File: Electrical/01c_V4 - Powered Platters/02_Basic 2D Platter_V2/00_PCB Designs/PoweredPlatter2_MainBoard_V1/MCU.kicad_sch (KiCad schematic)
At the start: 11 parts, among them J3 M20-7920242R, U1 STM32C071KBTx, Y1 16Mhz, 3.2 x 2.5

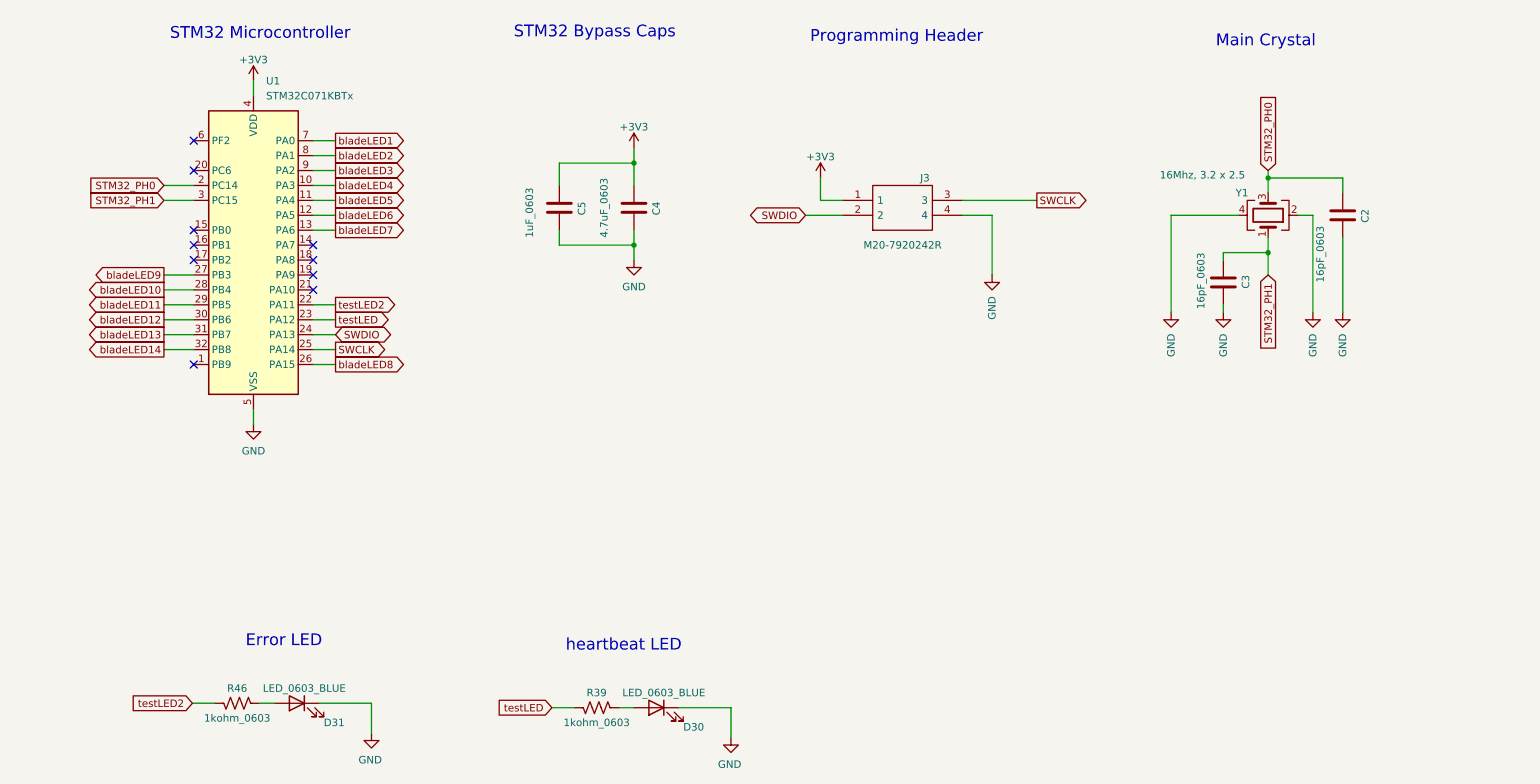
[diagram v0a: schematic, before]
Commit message: second powered platter main PCB designed and ready for CNC milling
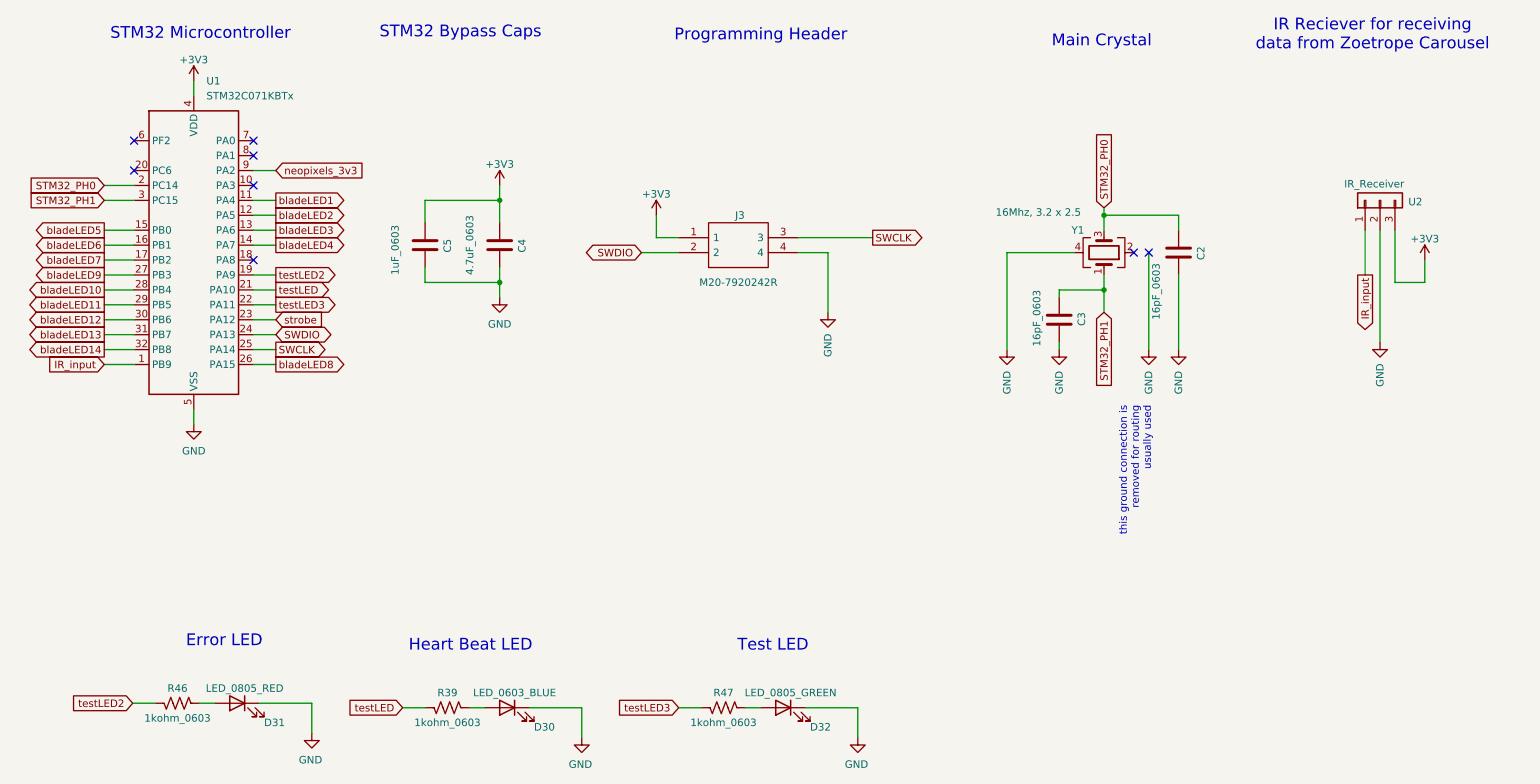
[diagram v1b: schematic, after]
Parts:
- added D32: LED_0805_GREEN, LED_SMD:LED_0805_2012Metric, symbol Device:LED
- added R47: 1kohm_0603, Resistor_SMD:R_0603_1608Metric, symbol Device:R_US
- added U2: IR_Receiver, Connector_PinHeader_2.54mm:PinHeader_1x03_P2.54mm_Vertical, symbol Connector_Generic:Conn_01x03
- D31: value LED_0603_BLUE -> LED_0805_RED; footprint LED_SMD:LED_0603_1608Metric -> LED_SMD:LED_0805_2012Metric
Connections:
- net +3V3: now also U2.3 (Pin_3)
- net GND: now also D32.1 (K), U2.2 (Pin_2); no longer Y1.2
- net bladeLED1: now also U1.11 (PA4); no longer U1.7 (PA0)
- net bladeLED2: now also U1.12 (PA5); no longer U1.8 (PA1)
- net bladeLED3: now also U1.13 (PA6); no longer U1.9 (PA2)
- net bladeLED4: now also U1.14 (PA7); no longer U1.10 (PA3)
- net bladeLED5: now also U1.15 (PB0); no longer U1.11 (PA4)
- net bladeLED6: now also U1.16 (PB1); no longer U1.12 (PA5)
- net bladeLED7: now also U1.17 (PB2); no longer U1.13 (PA6)
- net testLED: now also U1.21 (PA10); no longer U1.23 (PA12)
- net testLED2: now also U1.19 (PA9); no longer U1.22 (PA11)
- net IR_input: now reaches U1.1 (PB9)
- net IR_input: now also U2.1 (Pin_1)
- new net: D32.2 (A), R47.1
- new net neopixels_3v3: U1.9 (PA2)
- new net strobe: U1.23 (PA12)
- new net testLED3: R47.2, U1.22 (PA11)
- no-connect marks 10 -> 8
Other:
- note added: "Heart Beat LED"
- note added: "IR Reciever for receiving data from Zoetrope Carousel"
- note added: "Test LED"
- note added: "this ground connection is removed for routing usually used"
- note removed: "heartbeat LED"
- moved on the sheet: C2, C3, C4, C5, D30, D31, J3, R39, R46, Y1

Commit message: small updates - pushing to move to other computer
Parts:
- C2, C3, Y1: now not fitted
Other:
- note added: "DNP - Traces broke during CNC milling Use internal oscilator to save the headache"
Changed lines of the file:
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@@
 		)
 	)
+	(text "DNP - Traces broke during CNC milling\nUse internal oscilator to save the headache"
+		(exclude_from_sim no)
+		(at 185.42 67.056 0)
+		(effects
+			(font
+				(size 1.27 1.27)
+				(thickness 0.25)
+				(color 255 85 93 1)
+			)
+			(justify left bottom)
+		)
+	)
 	(text "STM32 Microcontroller"
 		(exclude_from_sim no)
@@
 		(on_board yes)
 		(in_pos_files yes)
-		(dnp no)
+		(dnp yes)
 		(property "Reference" "C2"
 			(at 222.25 90.17 90)
@@
 		(on_board yes)
 		(in_pos_files yes)
-		(dnp no)
+		(dnp yes)
 		(property "Reference" "C3"
 			(at 201.93 99.06 90)
@@
 		(on_board yes)
 		(in_pos_files yes)
-		(dnp no)
+		(dnp yes)
 		(property "Reference" "Y1"
 			(at 201.295 85.09 90)
